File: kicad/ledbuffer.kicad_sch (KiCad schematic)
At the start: 9 parts, among them J3 Conn_01x03, J4 Conn_01x03, J5 Conn_01x03, U1 LM2931-5.0_TO92

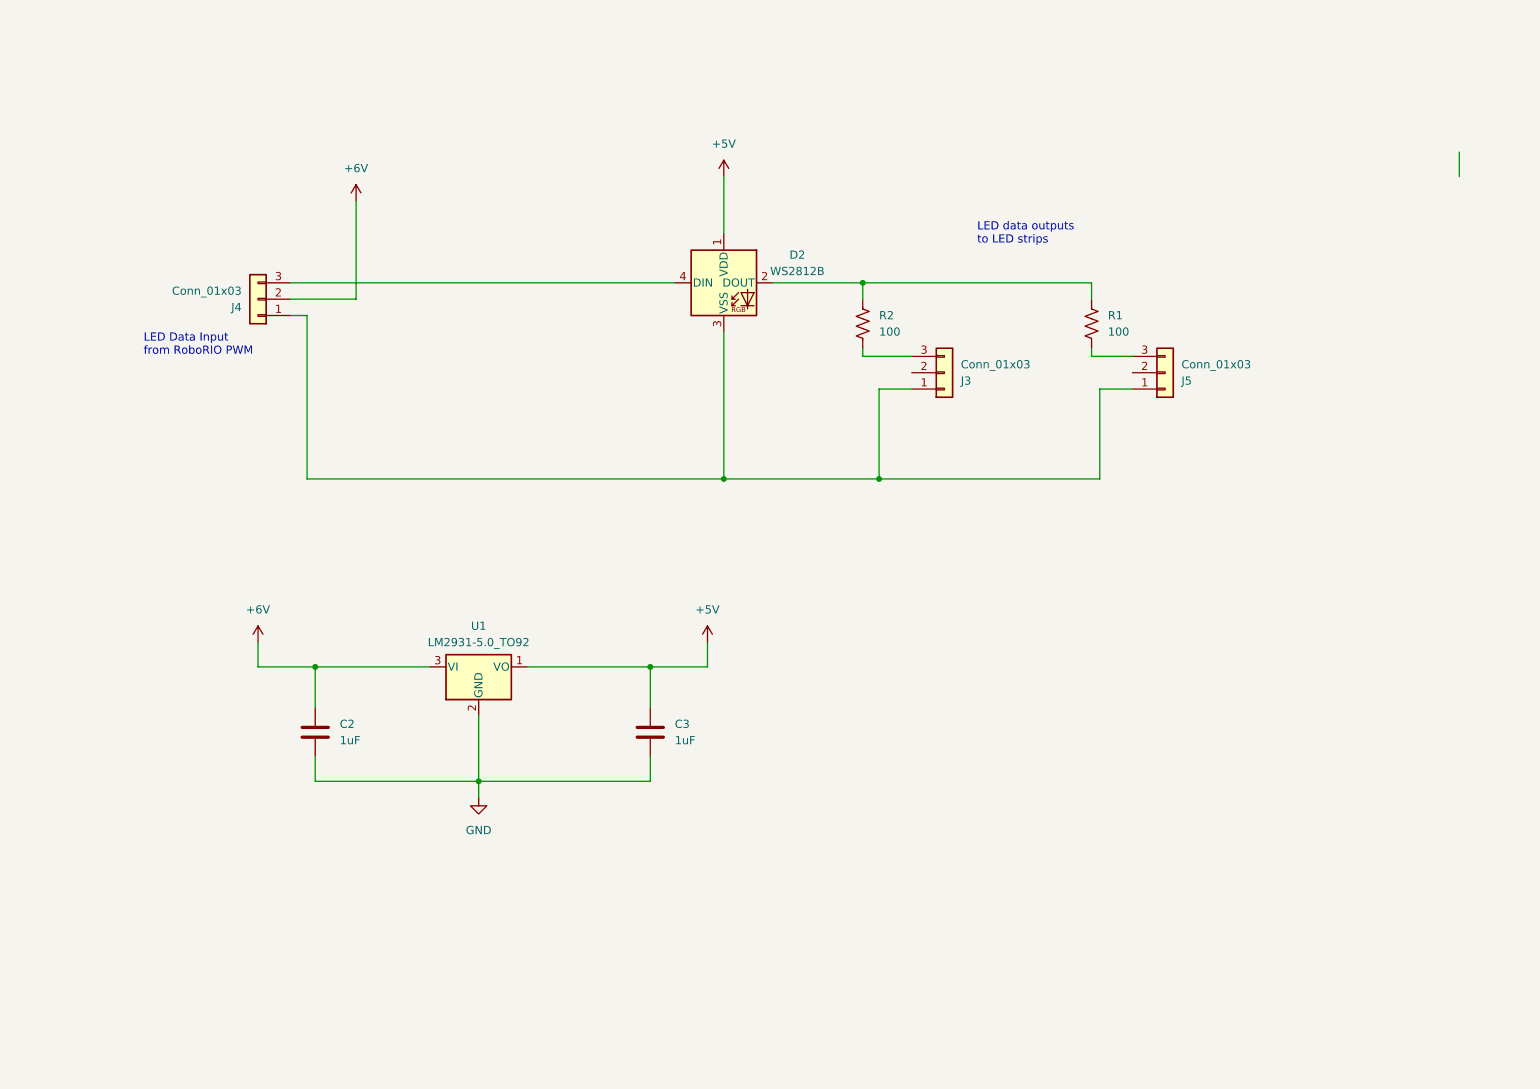
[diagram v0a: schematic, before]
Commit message: schematic updates, start doc/*, find footprints add a third output connector add power input connector, and polarity protection diode
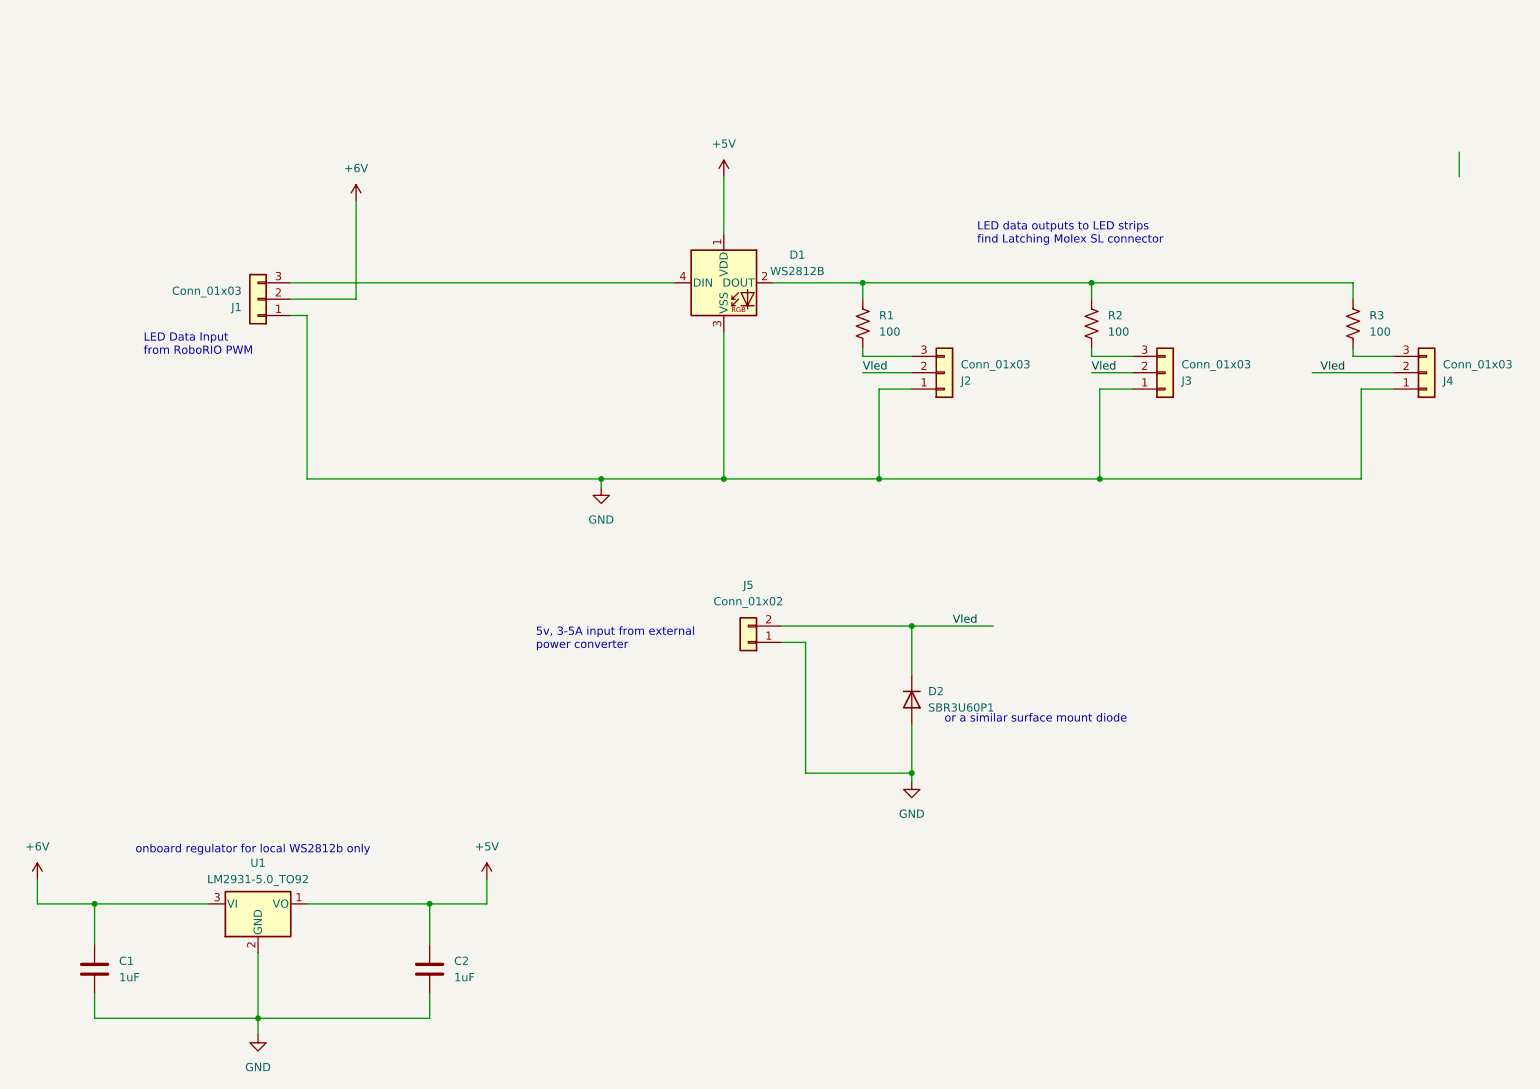
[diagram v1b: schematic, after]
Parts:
- added D2: SBR3U60P1, Diode_SMD:D_PowerDI-123, symbol Diode:1N4005
- added J4: Conn_01x03, symbol Connector_Generic:Conn_01x03
- added J5: Conn_01x02, symbol Connector_Generic:Conn_01x02
- added R3: 100, Resistor_SMD:R_0805_2012Metric_Pad1.20x1.40mm_HandSolder, symbol Device:R_US
- C1: renamed from C2; footprint (none) -> Capacitor_SMD:C_0805_2012Metric_Pad1.18x1.45mm_HandSolder
- C2: renamed from C3; footprint (none) -> Capacitor_SMD:C_0805_2012Metric_Pad1.18x1.45mm_HandSolder
- R1: renamed from R2; footprint (none) -> Resistor_SMD:R_0805_2012Metric_Pad1.20x1.40mm_HandSolder
- R2: renamed from R1; footprint (none) -> Resistor_SMD:R_0805_2012Metric_Pad1.20x1.40mm_HandSolder
- renumbered D2 to D1, J4 to J1, J3 to J2, J5 to J3
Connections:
- net GND: now also D1.3 (VSS), J1.1 (Pin_1), J2.1 (Pin_1), J3.1 (Pin_1), D2.2 (A), J4.1 (Pin_1), J5.1 (Pin_1)
- net at D1.2 (DOUT), R1.1, R2.1: now also R3.1
- net Vled: now reaches J3.2 (Pin_2)
- net Vled: now also J2.2 (Pin_2), D2.1 (K), J4.2 (Pin_2), J5.2 (Pin_2)
- new net: J4.3 (Pin_3), R3.2
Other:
- note added: "5v, 3-5A input from external power converter"
- note added: "LED data outputs to LED strips find Latching Molex SL connector"
- note added: "onboard regulator for local WS2812b only"
- note added: "or a similar surface mount diode"
- note removed: "LED data outputs to LED strips"
- moved on the sheet: C1, C2, U1

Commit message: candidate final schematic assigned footprints to all parts added more regulator output capacitors to satisfy datasheet requirements added another input connector.  only ground used.  only for mechanical stability.
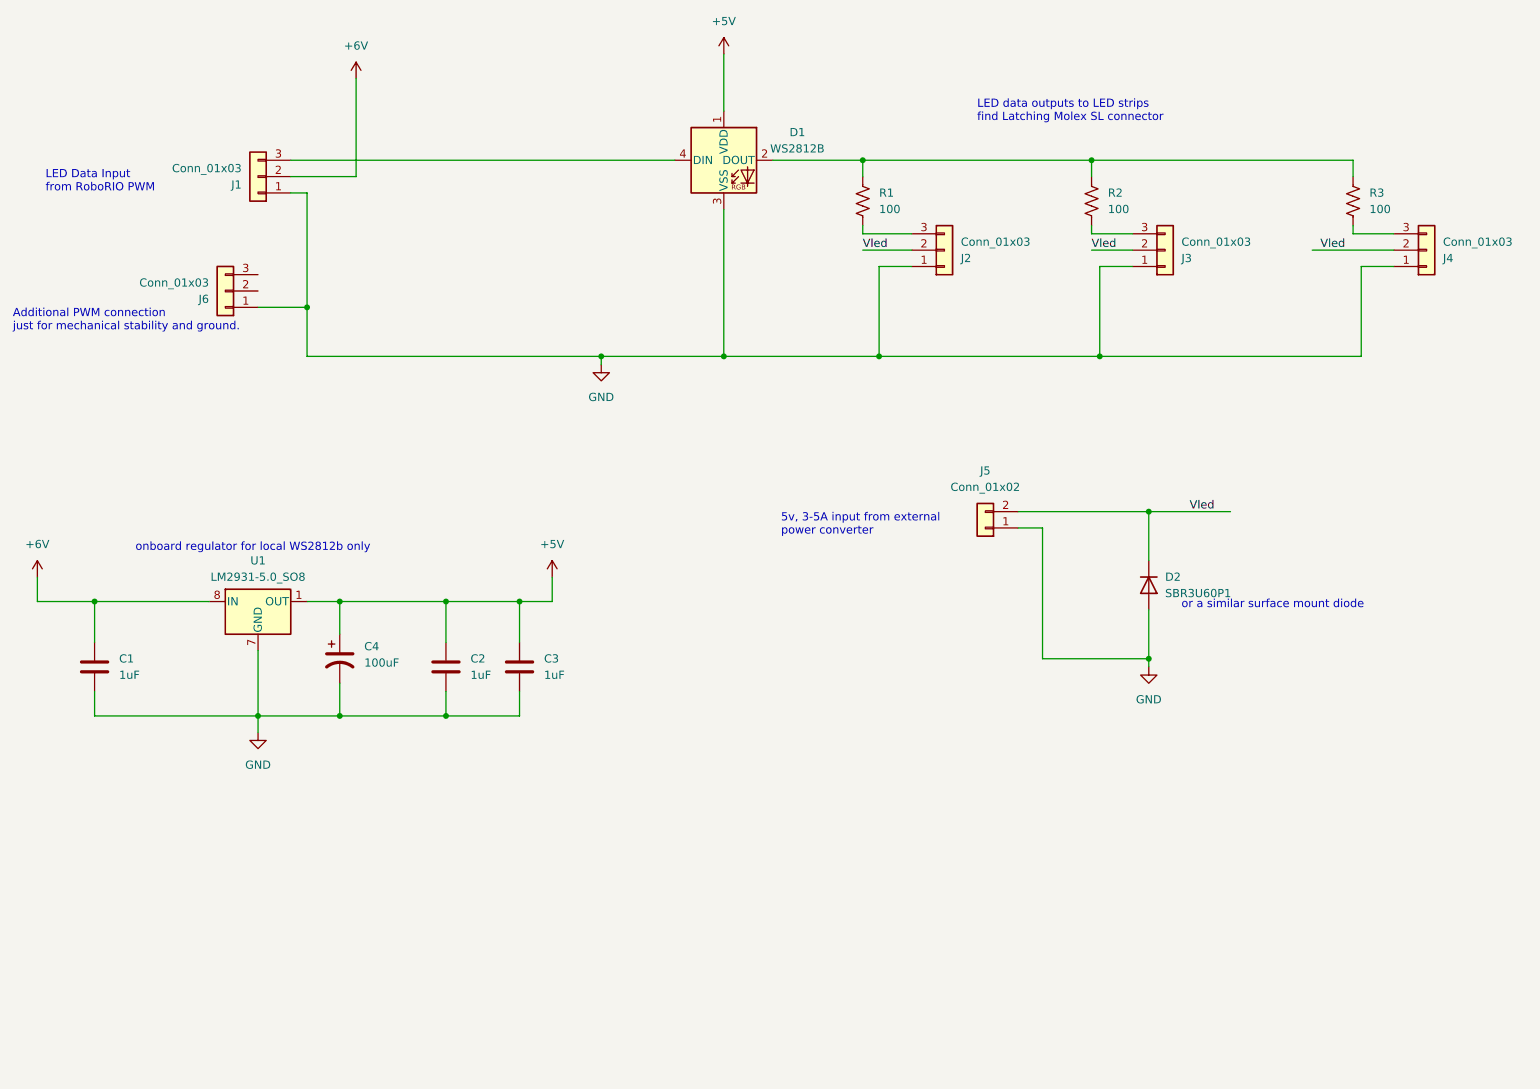
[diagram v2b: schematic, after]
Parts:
- removed U1: LM2931-5.0_TO92, Package_TO_SOT_THT:TO-92_Inline, symbol Regulator_Linear:LP2950-3.0_TO92
- added C3: 1uF, Capacitor_SMD:C_0805_2012Metric_Pad1.18x1.45mm_HandSolder, symbol Device:C
- added C4: 100uF, Capacitor_SMD:C_1206_3216Metric_Pad1.33x1.80mm_HandSolder, symbol Device:C_Polarized_US
- added J6: Conn_01x03, Connector_PinSocket_2.54mm:PinSocket_1x03_P2.54mm_Vertical, symbol Connector_Generic:Conn_01x03
- added U1: LM2931-5.0_SO8, Package_SO:SOIC-8_3.9x4.9mm_P1.27mm, symbol Regulator_Linear:LM2931-5.0_SO8
- J1: footprint (none) -> Connector_PinSocket_2.54mm:PinSocket_1x03_P2.54mm_Vertical
- J2, J3, J4: footprint (none) -> Library:CONN_70555-0002_MOL
- J5: footprint (none) -> Library:26011102
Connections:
- net +5V: now also C3.1, C4.1, U1.1 (OUT)
- net +6V: now also U1.8 (IN)
- net GND: now also C3.2, C4.2, J6.1 (Pin_1), U1.2 (GND), U1.3 (GND), U1.6 (GND), U1.7 (GND)
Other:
- note added: "Additional PWM connection just for mechanical stability and ground."
- moved on the sheet: C1, C2, D1, D2, J1, J2, J3, J4, J5, R1, R2, R3
